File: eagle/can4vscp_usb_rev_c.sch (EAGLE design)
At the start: 32 parts, among them IC1 PIC18LF26J50-I/SO, IC2 MCP2515, IC3 MCP2551SN, IC6 MCP23K256, IC7 MCP1603, J2 A00-108-220-450, J4 USB-B-S, Q1 12 MHZ

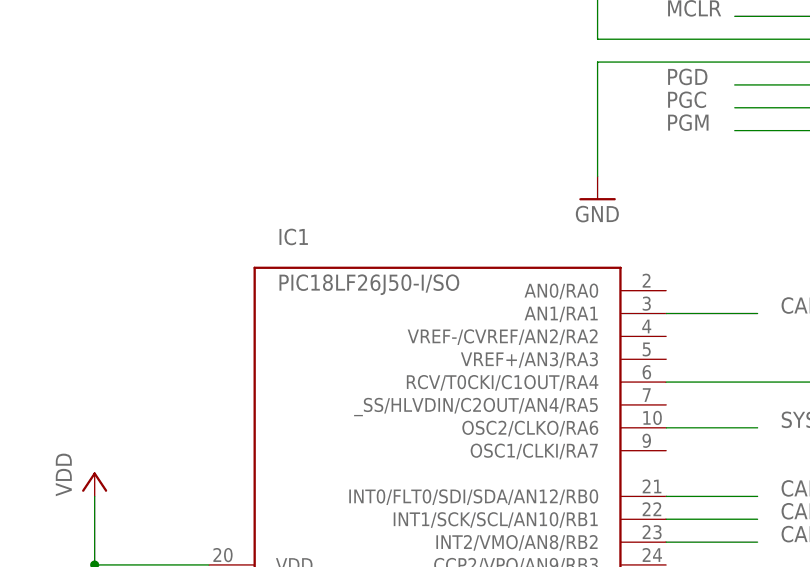
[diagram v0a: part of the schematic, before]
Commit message: Corrected processor type
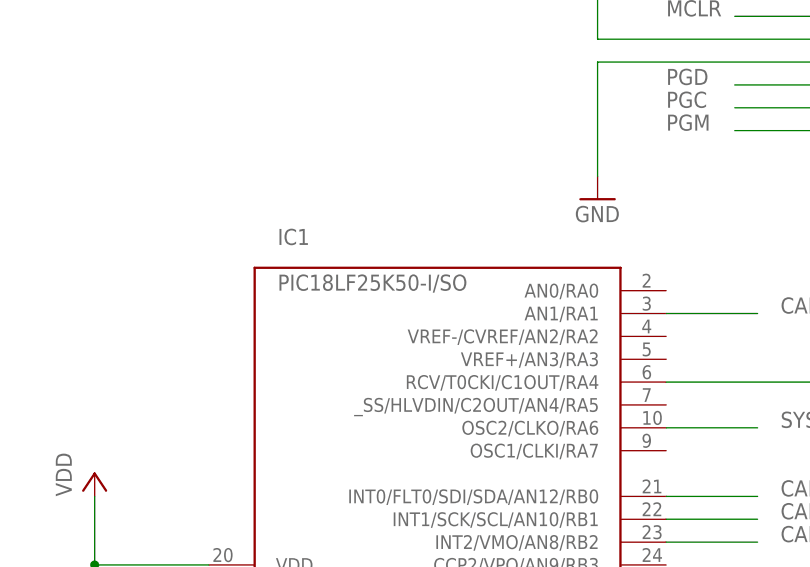
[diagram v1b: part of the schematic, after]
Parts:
- IC1: value PIC18LF26J50-I/SO -> PIC18LF25K50-I/SO
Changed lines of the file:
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@@
 <part name="C4" library="rcl" deviceset="C-EU" device="C0805" value="15pF"/>
 <part name="C6" library="rcl" deviceset="C-EU" device="C0805" value="15pF"/>
-<part name="IC1" library="microchip-pic18fxx5x" deviceset="PIC18*2550" device="-I/SO" technology="LF" value="PIC18LF26J50-I/SO"/>
+<part name="IC1" library="microchip-pic18fxx5x" deviceset="PIC18*2550" device="-I/SO" technology="LF" value="PIC18LF25K50-I/SO"/>
 <part name="P+2" library="SUPPLY1" deviceset="VCC" device="" value="VDD"/>
 <part name="GND17" library="SUPPLY1" deviceset="GND" device=""/>
